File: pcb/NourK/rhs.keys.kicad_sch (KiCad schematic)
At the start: 33 parts, among them SW1 Y, SW10 K, SW11 L, SW12 ;, SW13 ', SW14 ENTER, SW15 N, SW16 M, SW17 ,, SW18 ., SW19 /, SW2 U, SW20 RSHIFT, SW21 SPACE, SW22 LAYER, SW23 LAYER, SW24 LAYER, SW25 RCTRL, SW3 I, SW4 O, SW5 P, SW6 [, SW7 ], SW8 H, SW9 J

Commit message: Draft LHS tracks
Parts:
- D1, D8: value (none) -> BAV70SRAZ; footprint (none) -> Nour_KB:DIO_BAV70SRAZ
- D2: renamed from D3; value (none) -> BAV70SRAZ; footprint (none) -> Nour_KB:DIO_BAV70SRAZ
- D3: renamed from D5; value (none) -> BAV70SRAZ; footprint (none) -> Nour_KB:DIO_BAV70SRAZ
- D4: renamed from D7; value (none) -> BAV70SRAZ; footprint (none) -> Nour_KB:DIO_BAV70SRAZ
- D5: renamed from D2; value (none) -> BAV70SRAZ; footprint (none) -> Nour_KB:DIO_BAV70SRAZ
- D6: renamed from D4; value (none) -> BAV70SRAZ; footprint (none) -> Nour_KB:DIO_BAV70SRAZ
- D7: renamed from D6; value (none) -> BAV70SRAZ; footprint (none) -> Nour_KB:DIO_BAV70SRAZ
- SW10: renamed from SW22; footprint (none) -> Keebio-Parts:MX-Alps-Choc-1U-NoLED
- SW11: renamed from SW3; footprint (none) -> Keebio-Parts:MX-Alps-Choc-1U-NoLED
- SW12: renamed from SW10; footprint (none) -> Keebio-Parts:MX-Alps-Choc-1U-NoLED
- SW13: renamed from SW17; footprint (none) -> Keebio-Parts:MX-Alps-Choc-1U-NoLED
- SW14: renamed from SW23; footprint (none) -> Keebio-Parts:MX-Alps-Choc-1U-NoLED
- SW15: renamed from SW4; footprint (none) -> Keebio-Parts:MX-Alps-Choc-1U-NoLED
- SW16: renamed from SW11; footprint (none) -> Keebio-Parts:MX-Alps-Choc-1U-NoLED
- SW17: renamed from SW18; footprint (none) -> Keebio-Parts:MX-Alps-Choc-1U-NoLED
- SW18: renamed from SW24; footprint (none) -> Keebio-Parts:MX-Alps-Choc-1U-NoLED
- SW19: renamed from SW5; footprint (none) -> Keebio-Parts:MX-Alps-Choc-1U-NoLED
- SW20: renamed from SW12; footprint (none) -> Keebio-Parts:MX-Alps-Choc-1U-NoLED
- SW21: renamed from SW19; footprint (none) -> Keebio-Parts:MX-Alps-Choc-1U-NoLED
- SW22: renamed from SW25; footprint (none) -> Keebio-Parts:MX-Alps-Choc-1U-NoLED
- SW23: renamed from SW6; footprint (none) -> Keebio-Parts:MX-Alps-Choc-1U-NoLED
- SW24: renamed from SW13; footprint (none) -> Keebio-Parts:MX-Alps-Choc-1U-NoLED
- SW25: renamed from SW20; footprint (none) -> Keebio-Parts:MX-Alps-Choc-1U-NoLED
- SW26: renamed from SW7; footprint (none) -> Keebio-Parts:MX-Alps-Choc-1U-NoLED
- SW27: renamed from SW14; footprint (none) -> Keebio-Parts:MX-Alps-Choc-1U-NoLED
- SW3: renamed from SW1; footprint (none) -> Keebio-Parts:MX-Alps-Choc-1U-NoLED
- SW4: renamed from SW8; footprint (none) -> Keebio-Parts:MX-Alps-Choc-1U-NoLED
- SW5: renamed from SW15; footprint (none) -> Keebio-Parts:MX-Alps-Choc-1U-NoLED
- SW6: renamed from SW21; footprint (none) -> Keebio-Parts:MX-Alps-Choc-1U-NoLED
- SW7: renamed from SW2; footprint (none) -> Keebio-Parts:MX-Alps-Choc-1U-NoLED
- SW8: renamed from SW9; footprint (none) -> Keebio-Parts:MX-Alps-Choc-1U-NoLED
- SW9: renamed from SW16; footprint (none) -> Keebio-Parts:MX-Alps-Choc-1U-NoLED
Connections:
- net at SW10.1 (A): now also D4.4; no longer D4.2
- net at SW17.1 (A): now also D7.5; no longer D7.1
- net at SW19.1 (A): now also D5.4; no longer D5.2
- net at SW8.1 (A): now also D2.4; no longer D2.2
- net at SW14.1 (A): now also D4.2; no longer D4.4
- net at SW3.1 (A): now also D1.5; no longer D1.1
- net at SW11.1 (A): now also D1.2; no longer D1.4
- net at SW23.1 (A): now also D5.2; no longer D5.4
- net at D7.2: now also SW25.1 (A); no longer SW21.1 (A)
- net at D7.4: now also SW21.1 (A); no longer SW25.1 (A)
- net at SW24.1 (A): now also D6.2; no longer D6.4
- net at SW13.1 (A): now also D3.2; no longer D3.4
- net at SW16.1 (A): now also D6.5; no longer D6.1
- net at SW22.1 (A): now also D8.4; no longer D8.2
- net at D8.1: no longer SW18.1 (A)
- net at D8.5: now also SW18.1 (A)
- net at SW12.1 (A): now also D2.2; no longer D2.4
- net at SW5.1 (A): now also D3.5; no longer D3.1
- net at SW9.1 (A): now also D3.4; no longer D3.2
- net at SW26.1 (A): now also D5.1; no longer D5.5
- net at SW20.1 (A): now also D6.4; no longer D6.2
- net at SW4.1 (A): now also D2.5; no longer D2.1
- net at SW7.1 (A): now also D1.4; no longer D1.2
- net at SW27.1 (A): now also D6.1; no longer D6.5
- net at SW6.1 (A): now also D4.5; no longer D4.1
- net at SW15.1 (A): now also D5.5; no longer D5.1
- net KEY_COL10 renamed KEY.COL3
- net KEY_COL11 renamed KEY.COL4
- net KEY_COL12 renamed KEY.COL5
- net KEY_COL13 renamed KEY.COL6
- net KEY_COL14 renamed KEY.COL7
- net KEY_COL8 renamed KEY.COL1
- net KEY_COL9 renamed KEY.COL2
- net KEY_ROW1 renamed KEY.ROW1
- net KEY_ROW2 renamed KEY.ROW2
- net KEY_ROW3 renamed KEY.ROW3
- net KEY_ROW4 renamed KEY.ROW4

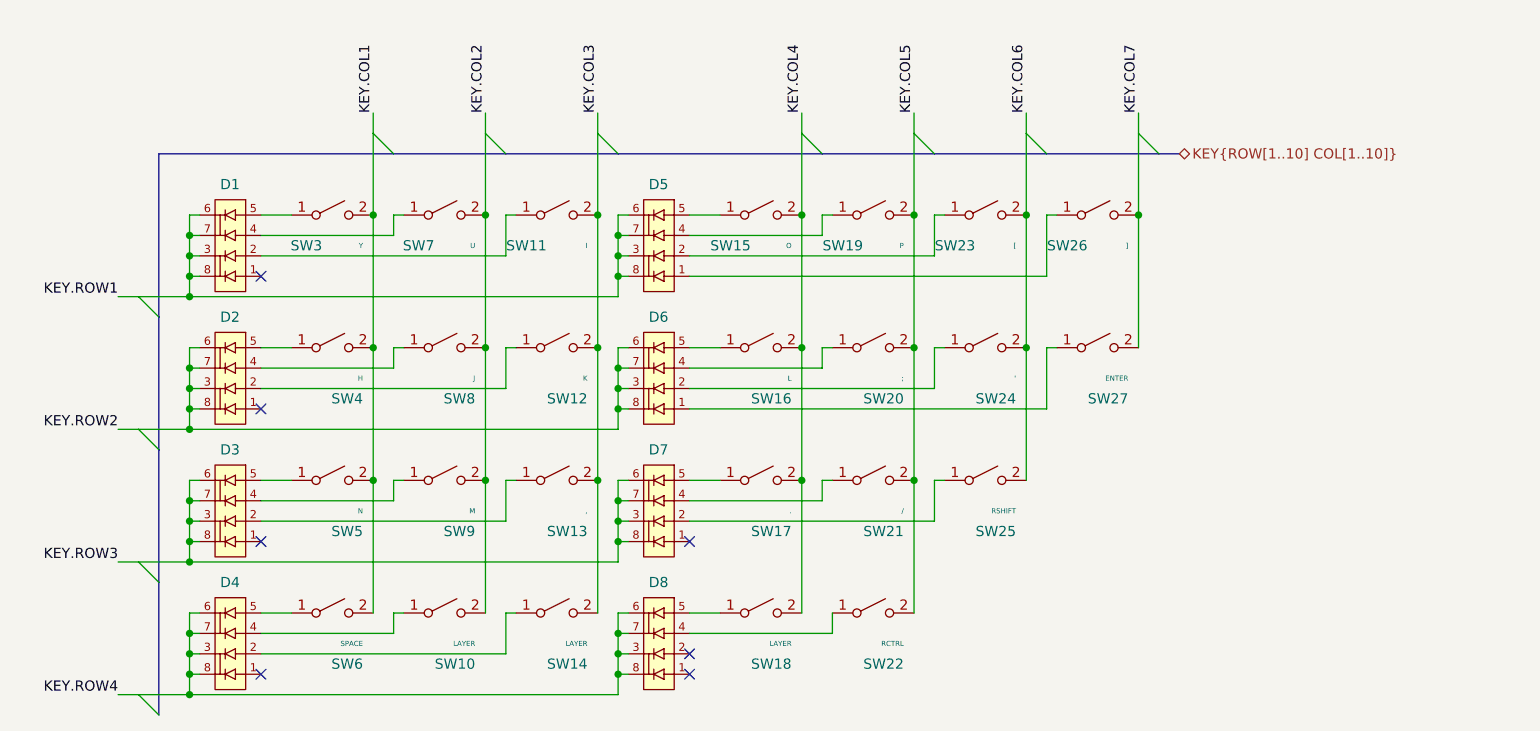
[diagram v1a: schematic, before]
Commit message: Re-traced RHS
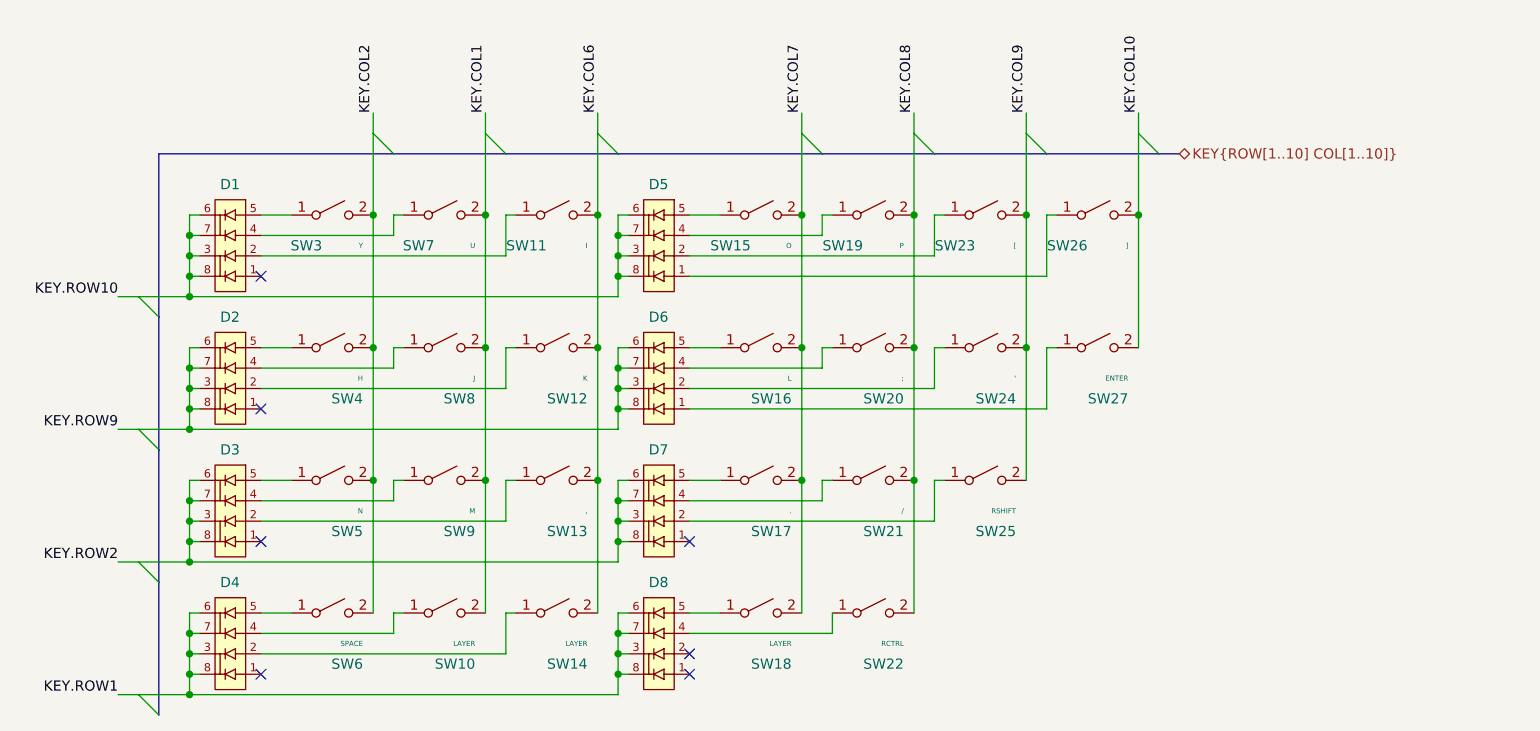
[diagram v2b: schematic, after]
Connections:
- net KEY.COL3 is gone; now on net KEY.COL6: SW11.2 (B), SW12.2 (B), SW13.2 (B), SW14.2 (B)
- net KEY.COL4 is gone; now on net KEY.COL7: SW15.2 (B), SW16.2 (B), SW17.2 (B), SW18.2 (B)
- net KEY.ROW3 is gone; now on net KEY.ROW2: D3.3, D3.6, D3.7, D3.8, D7.3, D7.6, D7.7, D7.8
- net KEY.ROW4 is gone; now on net KEY.ROW1: D4.3, D4.6, D4.7, D4.8, D8.3, D8.6, D8.7, D8.8
- net KEY.COL1: now also SW10.2 (B), SW7.2 (B), SW8.2 (B), SW9.2 (B); no longer SW3.2 (B), SW4.2 (B), SW5.2 (B), SW6.2 (B)
- net KEY.COL2: now also SW3.2 (B), SW4.2 (B), SW5.2 (B), SW6.2 (B); no longer SW10.2 (B), SW7.2 (B), SW8.2 (B), SW9.2 (B)
- net KEY.COL6: no longer SW23.2 (B), SW24.2 (B), SW25.2 (B)
- net KEY.COL7: no longer SW26.2 (B), SW27.2 (B)
- net KEY.ROW1: no longer D1.3, D1.6, D1.7, D1.8, D5.3, D5.6, D5.7, D5.8
- net KEY.ROW2: no longer D2.3, D2.6, D2.7, D2.8, D6.3, D6.6, D6.7, D6.8
- net KEY.COL5 renamed KEY.COL8
- new net KEY.COL10: SW26.2 (B), SW27.2 (B)
- new net KEY.COL9: SW23.2 (B), SW24.2 (B), SW25.2 (B)
- new net KEY.ROW10: D1.3, D1.6, D1.7, D1.8, D5.3, D5.6, D5.7, D5.8
- new net KEY.ROW9: D2.3, D2.6, D2.7, D2.8, D6.3, D6.6, D6.7, D6.8
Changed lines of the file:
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@@
     (stroke (width 0) (type default) (color 0 0 0 0))
   )
-  (label "KEY.COL1" (at 101.6 59.69 90)
+  (label "KEY.COL2" (at 101.6 59.69 90)
     (effects (font (size 1.27 1.27)) (justify left bottom))
   )
-  (label "KEY.ROW1" (at 69.85 82.55 180)
+  (label "KEY.ROW10" (at 69.85 82.55 180)
     (effects (font (size 1.27 1.27)) (justify right bottom))
   )
-  (label "KEY.ROW4" (at 69.85 132.08 180)
+  (label "KEY.ROW1" (at 69.85 132.08 180)
     (effects (font (size 1.27 1.27)) (justify right bottom))
   )
-  (label "KEY.COL5" (at 168.91 59.69 90)
+  (label "KEY.COL8" (at 168.91 59.69 90)
     (effects (font (size 1.27 1.27)) (justify left bottom))
   )
-  (label "KEY.ROW3" (at 69.85 115.57 180)
+  (label "KEY.ROW2" (at 69.85 115.57 180)
     (effects (font (size 1.27 1.27)) (justify right bottom))
   )
-  (label "KEY.COL4" (at 154.94 59.69 90)
+  (label "KEY.COL7" (at 154.94 59.69 90)
     (effects (font (size 1.27 1.27)) (justify left bottom))
   )
-  (label "KEY.COL6" (at 182.88 59.69 90)
+  (label "KEY.COL9" (at 182.88 59.69 90)
     (effects (font (size 1.27 1.27)) (justify left bottom))
   )
-  (label "KEY.COL2" (at 115.57 59.69 90)
+  (label "KEY.COL1" (at 115.57 59.69 90)
     (effects (font (size 1.27 1.27)) (justify left bottom))
   )
-  (label "KEY.ROW2" (at 69.85 99.06 180)
+  (label "KEY.ROW9" (at 69.85 99.06 180)
     (effects (font (size 1.27 1.27)) (justify right bottom))
   )
-  (label "KEY.COL7" (at 196.85 59.69 90)
+  (label "KEY.COL10" (at 196.85 59.69 90)
     (effects (font (size 1.27 1.27)) (justify left bottom))
   )
-  (label "KEY.COL3" (at 129.54 59.69 90)
+  (label "KEY.COL6" (at 129.54 59.69 90)
     (effects (font (size 1.27 1.27)) (justify left bottom))
   )

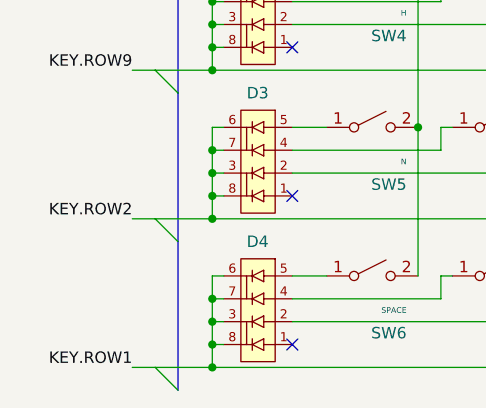
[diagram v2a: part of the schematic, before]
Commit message: RHS and LHS wire complete and initial DRC
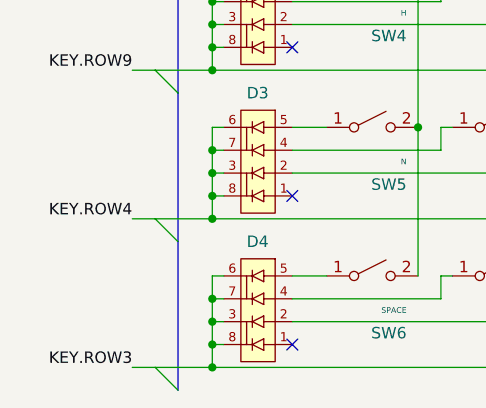
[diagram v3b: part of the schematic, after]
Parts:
- SW10, SW11, SW12, SW13, SW14, SW15, SW16, SW17, SW18, SW19, SW20, SW21, SW22, SW23, SW24, SW25, SW26, SW27, SW3, SW4, SW5, SW6, SW7, SW8, SW9: footprint Keebio-Parts:MX-Alps-Choc-1U-NoLED -> Nour_KB:MX_Choc_1U
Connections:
- net KEY.ROW1 renamed KEY.ROW3
- net KEY.ROW2 renamed KEY.ROW4
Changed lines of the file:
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@@
     (effects (font (size 1.27 1.27)) (justify right bottom))
   )
-  (label "KEY.ROW1" (at 69.85 132.08 180)
+  (label "KEY.ROW3" (at 69.85 132.08 180)
     (effects (font (size 1.27 1.27)) (justify right bottom))
   )
@@
     (effects (font (size 1.27 1.27)) (justify left bottom))
   )
-  (label "KEY.ROW2" (at 69.85 115.57 180)
+  (label "KEY.ROW4" (at 69.85 115.57 180)
     (effects (font (size 1.27 1.27)) (justify right bottom))
   )
@@
       (effects (font (size 0.63 0.63)) (justify right))
     )
-    (property "Footprint" "Keebio-Parts:MX-Alps-Choc-1U-NoLED" (id 2) (at 110.49 121.92 0)
+    (property "Footprint" "Nour_KB:MX_Choc_1U" (id 2) (at 110.49 121.92 0)
       (effects (font (size 1.27 1.27)) hide)
     )
@@
       (effects (font (size 0.63 0.63)) (justify right))
     )
-    (property "Footprint" "Keebio-Parts:MX-Alps-Choc-1U-NoLED" (id 2) (at 149.86 105.41 0)
+    (property "Footprint" "Nour_KB:MX_Choc_1U" (id 2) (at 149.86 105.41 0)
       (effects (font (size 1.27 1.27)) hide)
     )
@@
       (effects (font (size 0.63 0.63)) (justify right))
     )
-    (property "Footprint" "Keebio-Parts:MX-Alps-Choc-1U-NoLED" (id 2) (at 163.83 72.39 0)
+    (property "Footprint" "Nour_KB:MX_Choc_1U" (id 2) (at 163.83 72.39 0)
       (effects (font (size 1.27 1.27)) hide)
     )
@@
       (effects (font (size 0.63 0.63)) (justify right))
     )
-    (property "Footprint" "Keebio-Parts:MX-Alps-Choc-1U-NoLED" (id 2) (at 110.49 88.9 0)
+    (property "Footprint" "Nour_KB:MX_Choc_1U" (id 2) (at 110.49 88.9 0)
       (effects (font (size 1.27 1.27)) hide)
     )
@@
       (effects (font (size 0.63 0.63)) (justify right))
     )
-    (property "Footprint" "Keebio-Parts:MX-Alps-Choc-1U-NoLED" (id 2) (at 124.46 121.92 0)
+    (property "Footprint" "Nour_KB:MX_Choc_1U" (id 2) (at 124.46 121.92 0)
       (effects (font (size 1.27 1.27)) hide)
     )
@@
       (effects (font (size 0.63 0.63)) (justify right))
     )
-    (property "Footprint" "Keebio-Parts:MX-Alps-Choc-1U-NoLED" (id 2) (at 96.52 72.39 0)
+    (property "Footprint" "Nour_KB:MX_Choc_1U" (id 2) (at 96.52 72.39 0)
       (effects (font (size 1.27 1.27)) hide)
     )
@@
       (effects (font (size 0.63 0.63)) (justify right))
     )
-    (property "Footprint" "Keebio-Parts:MX-Alps-Choc-1U-NoLED" (id 2) (at 124.46 72.39 0)
+    (property "Footprint" "Nour_KB:MX_Choc_1U" (id 2) (at 124.46 72.39 0)
       (effects (font (size 1.27 1.27)) hide)
     )
@@
       (effects (font (size 0.63 0.63)) (justify right))
     )
-    (property "Footprint" "Keebio-Parts:MX-Alps-Choc-1U-NoLED" (id 2) (at 177.8 72.39 0)
+    (property "Footprint" "Nour_KB:MX_Choc_1U" (id 2) (at 177.8 72.39 0)
       (effects (font (size 1.27 1.27)) hide)
     )
@@
       (effects (font (size 0.63 0.63)) (justify right))
     )
-    (property "Footprint" "Keebio-Parts:MX-Alps-Choc-1U-NoLED" (id 2) (at 177.8 88.9 0)
+    (property "Footprint" "Nour_KB:MX_Choc_1U" (id 2) (at 177.8 88.9 0)
       (effects (font (size 1.27 1.27)) hide)
     )
@@
       (effects (font (size 0.63 0.63)) (justify right))
     )
-    (property "Footprint" "Keebio-Parts:MX-Alps-Choc-1U-NoLED" (id 2) (at 124.46 105.41 0)
+    (property "Footprint" "Nour_KB:MX_Choc_1U" (id 2) (at 124.46 105.41 0)
       (effects (font (size 1.27 1.27)) hide)
     )
@@
       (effects (font (size 0.63 0.63)) (justify right))
     )
-    (property "Footprint" "Keebio-Parts:MX-Alps-Choc-1U-NoLED" (id 2) (at 149.86 88.9 0)
+    (property "Footprint" "Nour_KB:MX_Choc_1U" (id 2) (at 149.86 88.9 0)
       (effects (font (size 1.27 1.27)) hide)
     )
@@
       (effects (font (size 0.63 0.63)) (justify right))
     )
-    (property "Footprint" "Keebio-Parts:MX-Alps-Choc-1U-NoLED" (id 2) (at 163.83 121.92 0)
+    (property "Footprint" "Nour_KB:MX_Choc_1U" (id 2) (at 163.83 121.92 0)
       (effects (font (size 1.27 1.27)) hide)
     )
@@
       (effects (font (size 0.63 0.63)) (justify right))
     )
-    (property "Footprint" "Keebio-Parts:MX-Alps-Choc-1U-NoLED" (id 2) (at 124.46 88.9 0)
+    (property "Footprint" "Nour_KB:MX_Choc_1U" (id 2) (at 124.46 88.9 0)
       (effects (font (size 1.27 1.27)) hide)
     )
@@
       (effects (font (size 0.63 0.63)) (justify right))
     )
-    (property "Footprint" "Keebio-Parts:MX-Alps-Choc-1U-NoLED" (id 2) (at 96.52 105.41 0)
+    (property "Footprint" "Nour_KB:MX_Choc_1U" (id 2) (at 96.52 105.41 0)
       (effects (font (size 1.27 1.27)) hide)
     )
@@
       (effects (font (size 0.63 0.63)) (justify right))
     )
-    (property "Footprint" "Keebio-Parts:MX-Alps-Choc-1U-NoLED" (id 2) (at 191.77 72.39 0)
+    (property "Footprint" "Nour_KB:MX_Choc_1U" (id 2) (at 191.77 72.39 0)
       (effects (font (size 1.27 1.27)) hide)
     )
@@
       (effects (font (size 0.63 0.63)) (justify right))
     )
-    (property "Footprint" "Keebio-Parts:MX-Alps-Choc-1U-NoLED" (id 2) (at 163.83 88.9 0)
+    (property "Footprint" "Nour_KB:MX_Choc_1U" (id 2) (at 163.83 88.9 0)
       (effects (font (size 1.27 1.27)) hide)
     )
@@
       (effects (font (size 0.63 0.63)) (justify right))
     )
-    (property "Footprint" "Keebio-Parts:MX-Alps-Choc-1U-NoLED" (id 2) (at 96.52 88.9 0)
+    (property "Footprint" "Nour_KB:MX_Choc_1U" (id 2) (at 96.52 88.9 0)
       (effects (font (size 1.27 1.27)) hide)
     )
@@
       (effects (font (size 0.63 0.63)) (justify right))
     )
-    (property "Footprint" "Keebio-Parts:MX-Alps-Choc-1U-NoLED" (id 2) (at 96.52 121.92 0)
+    (property "Footprint" "Nour_KB:MX_Choc_1U" (id 2) (at 96.52 121.92 0)
       (effects (font (size 1.27 1.27)) hide)
     )
@@
       (effects (font (size 0.63 0.63)) (justify right))
     )
-    (property "Footprint" "Keebio-Parts:MX-Alps-Choc-1U-NoLED" (id 2) (at 177.8 105.41 0)
+    (property "Footprint" "Nour_KB:MX_Choc_1U" (id 2) (at 177.8 105.41 0)
       (effects (font (size 1.27 1.27)) hide)
     )
@@
       (effects (font (size 0.63 0.63)) (justify right))
     )
-    (property "Footprint" "Keebio-Parts:MX-Alps-Choc-1U-NoLED" (id 2) (at 110.49 72.39 0)
+    (property "Footprint" "Nour_KB:MX_Choc_1U" (id 2) (at 110.49 72.39 0)
       (effects (font (size 1.27 1.27)) hide)
     )
@@
       (effects (font (size 0.63 0.63)) (justify right))
     )
-    (property "Footprint" "Keebio-Parts:MX-Alps-Choc-1U-NoLED" (id 2) (at 149.86 72.39 0)
+    (property "Footprint" "Nour_KB:MX_Choc_1U" (id 2) (at 149.86 72.39 0)
       (effects (font (size 1.27 1.27)) hide)
     )
@@
       (effects (font (size 0.63 0.63)) (justify right))
     )
-    (property "Footprint" "Keebio-Parts:MX-Alps-Choc-1U-NoLED" (id 2) (at 163.83 105.41 0)
+    (property "Footprint" "Nour_KB:MX_Choc_1U" (id 2) (at 163.83 105.41 0)
       (effects (font (size 1.27 1.27)) hide)
     )
@@
       (effects (font (size 0.63 0.63)) (justify right))
     )
-    (property "Footprint" "Keebio-Parts:MX-Alps-Choc-1U-NoLED" (id 2) (at 149.86 121.92 0)
+    (property "Footprint" "Nour_KB:MX_Choc_1U" (id 2) (at 149.86 121.92 0)
       (effects (font (size 1.27 1.27)) hide)
     )
@@
       (effects (font (size 0.63 0.63)) (justify right))
     )
-    (property "Footprint" "Keebio-Parts:MX-Alps-Choc-1U-NoLED" (id 2) (at 110.49 105.41 0)
+    (property "Footprint" "Nour_KB:MX_Choc_1U" (id 2) (at 110.49 105.41 0)
       (effects (font (size 1.27 1.27)) hide)
     )
@@
       (effects (font (size 0.63 0.63)) (justify right))
     )
-    (property "Footprint" "Keebio-Parts:MX-Alps-Choc-1U-NoLED" (id 2) (at 191.77 88.9 0)
-      (effects (font (size 1.27 1.27)) hide)
-    )
+    (property "Footprint" "Nour_KB:MX_Choc_1U" (id 2) (at 191.77 88.9 0)
+      (effects (font (size 1.27 1.27)) hide)
+    )

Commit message: Complete wiring
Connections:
- net KEY.ROW10 renamed KEY.ROW8
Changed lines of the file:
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@@
     (effects (font (size 1.27 1.27)) (justify left bottom))
   )
-  (label "KEY.ROW10" (at 69.85 82.55 180)
+  (label "KEY.ROW8" (at 69.85 82.55 180)
     (effects (font (size 1.27 1.27)) (justify right bottom))
   )
